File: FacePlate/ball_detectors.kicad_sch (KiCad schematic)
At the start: 38 parts, among them U4 LM393

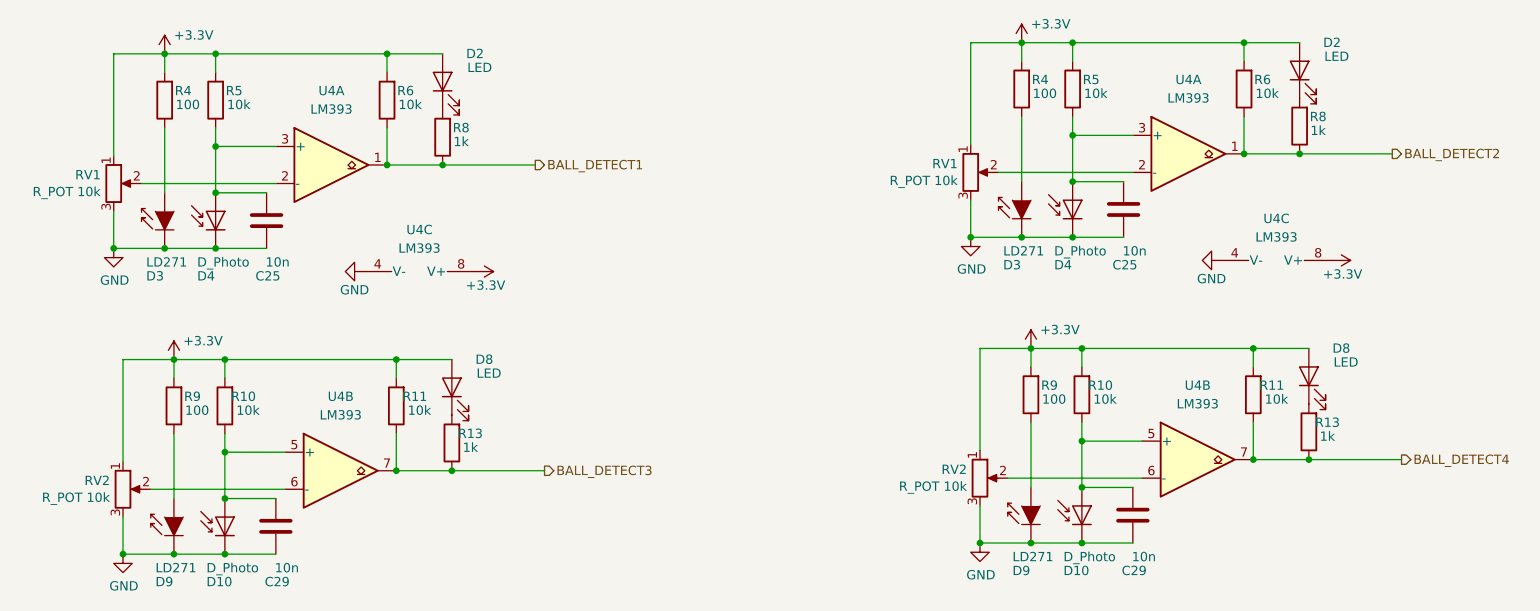
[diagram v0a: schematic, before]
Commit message: wip faceplate 2.0 schematic
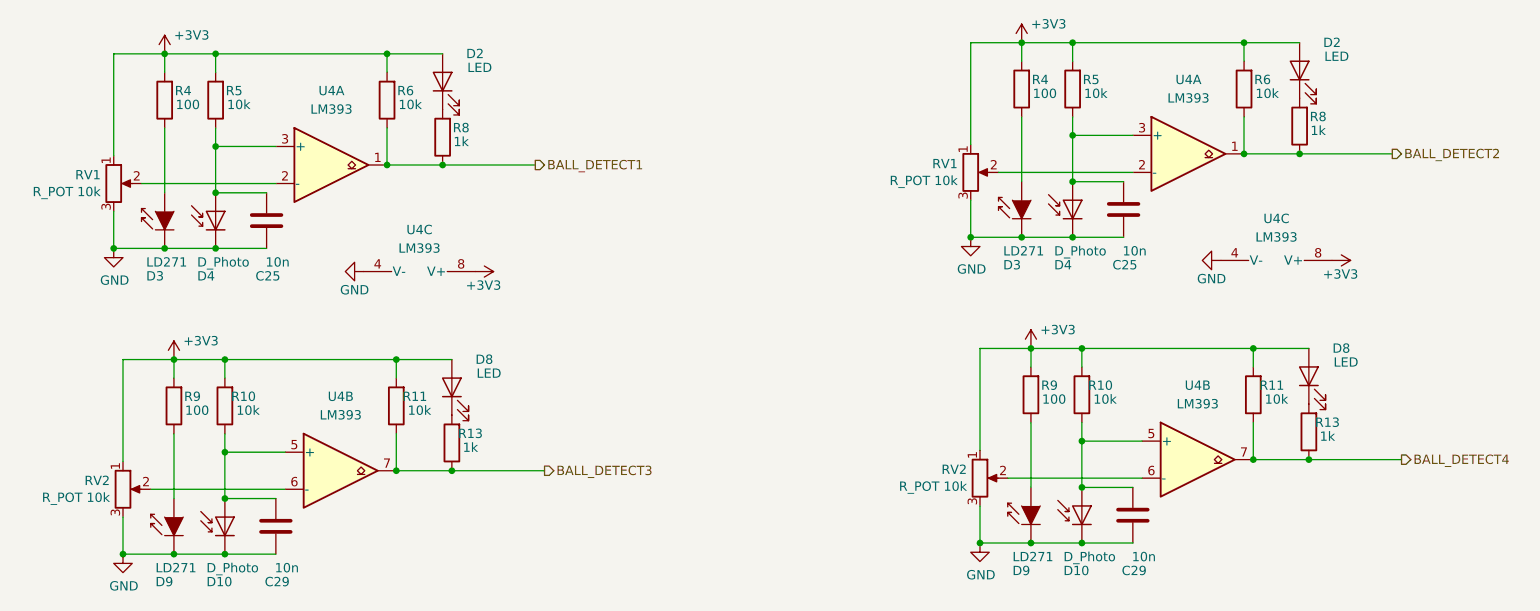
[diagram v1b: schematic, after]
